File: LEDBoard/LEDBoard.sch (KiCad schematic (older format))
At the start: 10 parts, among them P101 CONN_01X02, P102 CONN_01X02, P103 CONN_01X02, P104 CONN_01X02, P105 CONN_01X02, P106 CONN_01X02, P107 connector to 18650 batteries, P108 CONN_01X04, P109 CONN_01X06, P110 CONN_01X04

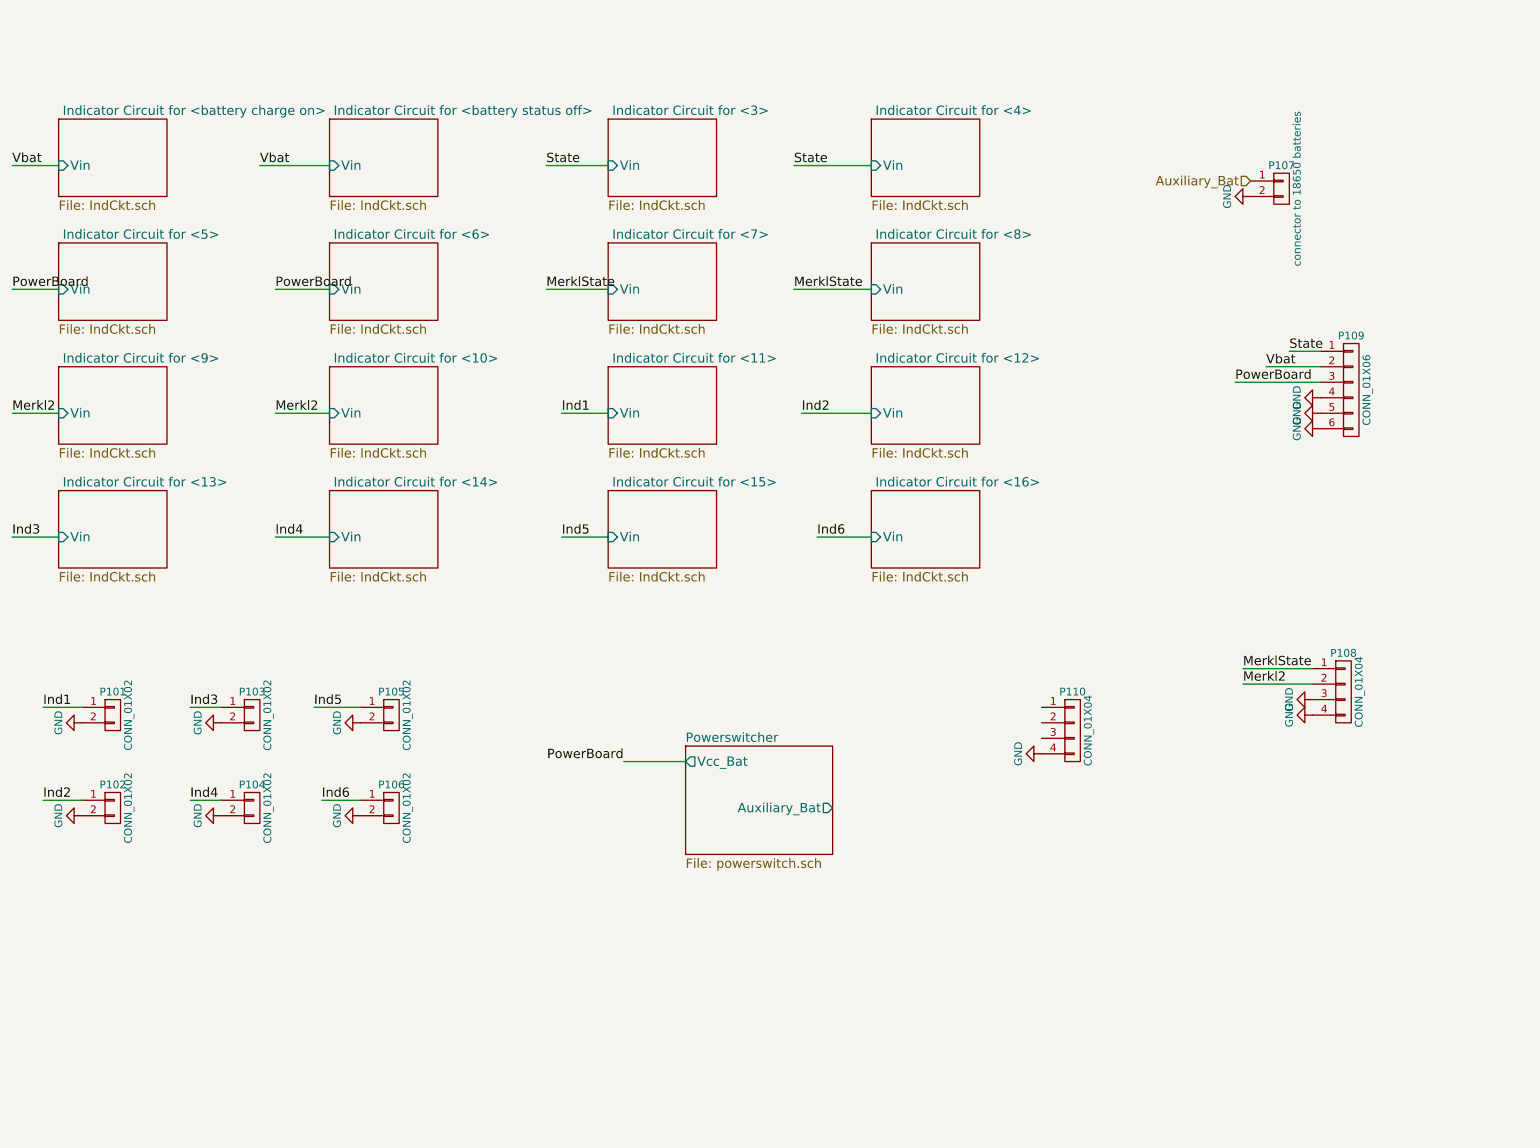
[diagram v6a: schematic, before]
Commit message: added more modules to the Led board and put in the circuit for the cool switch and the Led that goes along with it. Also made some more changes to the sensors and which ones we are going to have
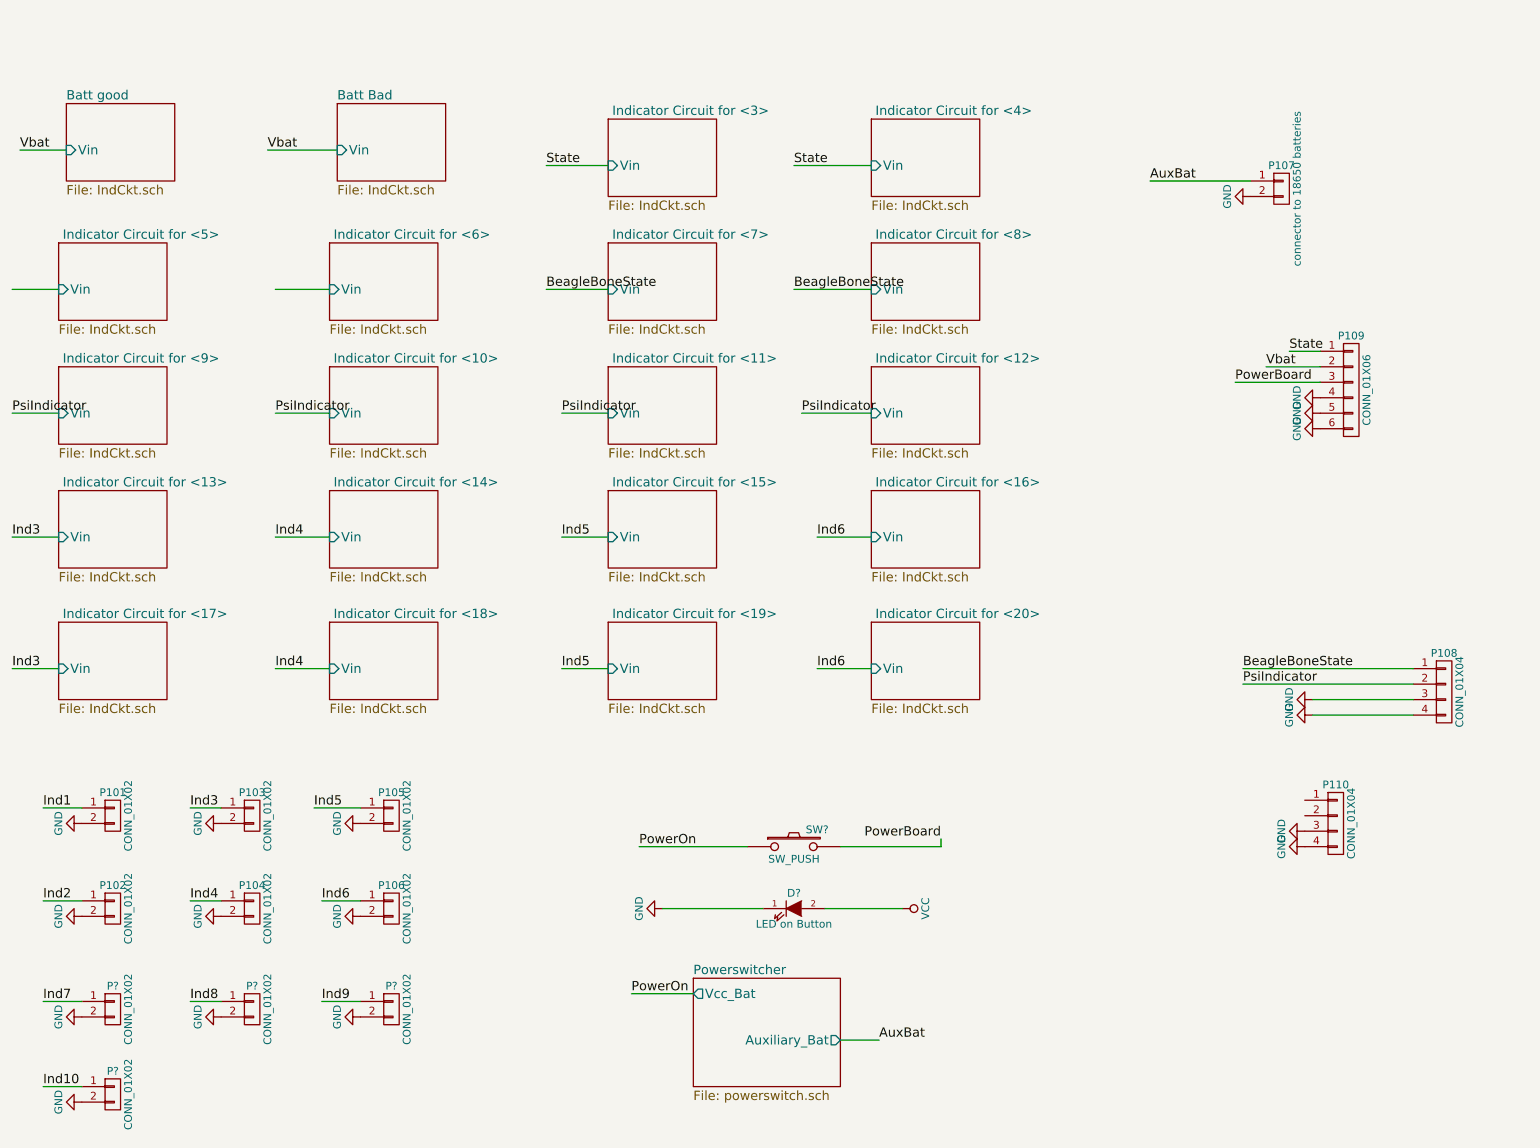
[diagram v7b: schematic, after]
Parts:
- added D?: LED on Button, symbol LED
- added P? (x4): CONN_01X02, hyperCustom:CONN_PHOENIX_1844210_2PIN, symbol CONN_01X02
- added SW?: SW_PUSH, symbol SW_PUSH
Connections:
- net labels added: AuxBat, BeagleBoneState, Ind10, Ind7, Ind8, Ind9, PowerOn, PsiIndicator, VCC
- net labels removed: Auxiliary_Bat, Merkl2, MerklState
- wire segments 28 -> 45
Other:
- moved on the sheet: P101, P102, P103, P104, P105, P106, P108, P110
